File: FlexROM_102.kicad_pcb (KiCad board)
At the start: 2 copper layers, 16.4 x 34.2 mm, 5 parts, among them J1 27C256 DIP LEGS, U1 28C256

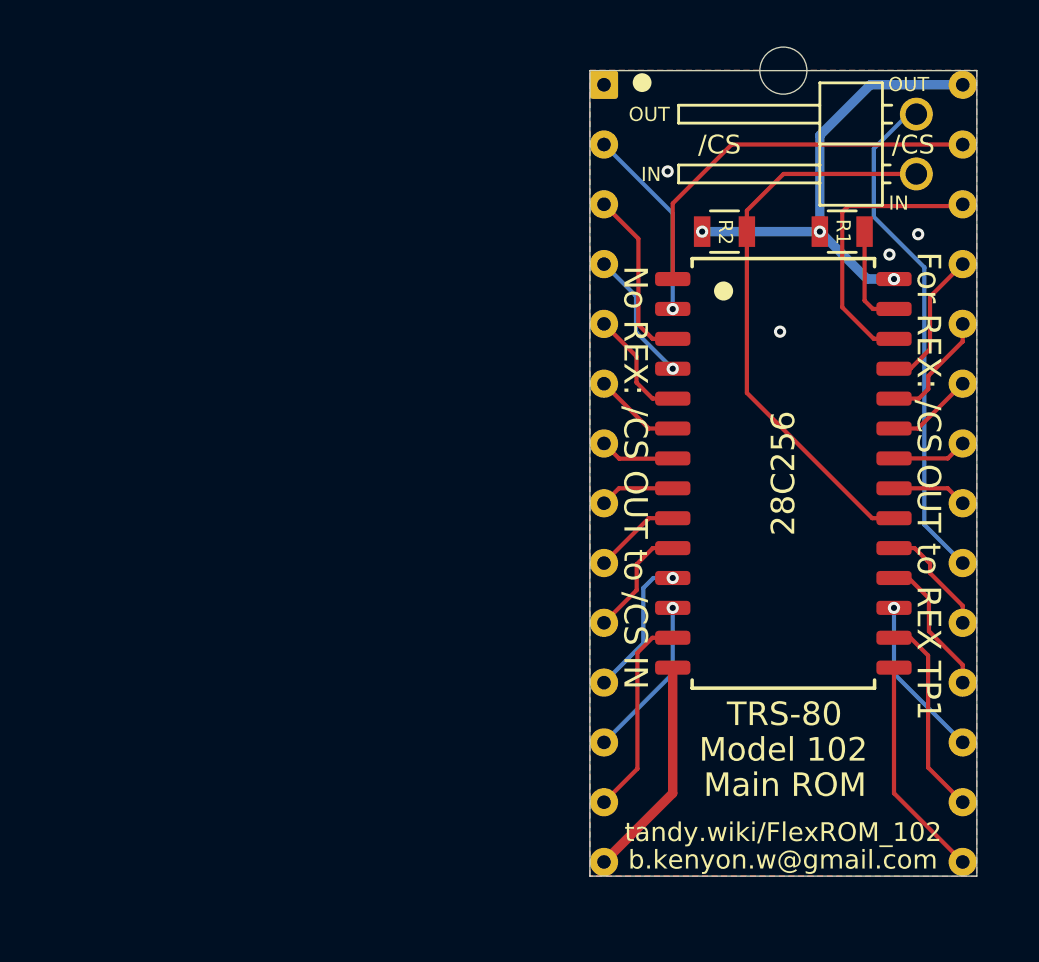
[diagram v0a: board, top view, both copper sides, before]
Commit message: FlexROM_100 programming adapter, FlexROM_102 programming jumpers
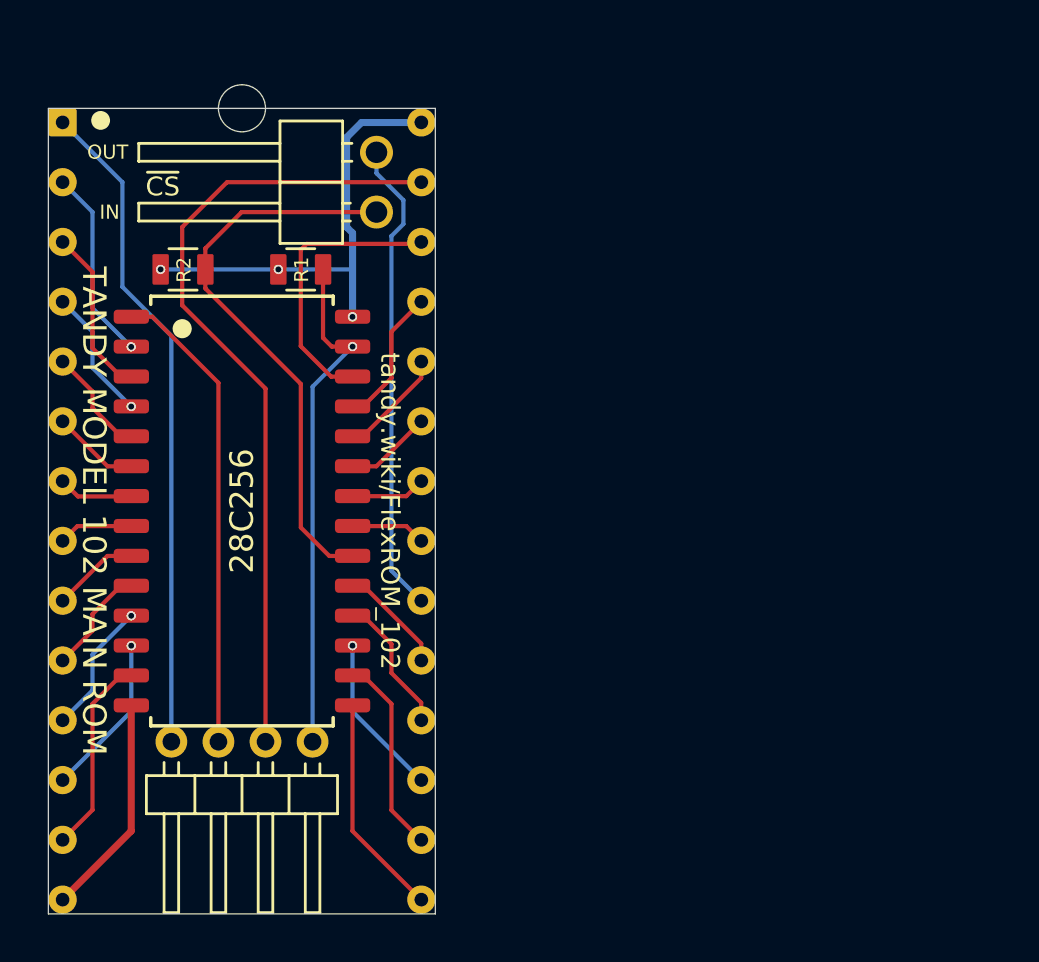
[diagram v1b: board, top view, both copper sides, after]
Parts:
- added JP2: Jumper_4_Bridged23, 000_LOCAL:PinHeader_1x04_P2.00mm_Horizontal, F.Cu at (130.0, 111.4)
- J1: footprint 000_LOCAL:DIP-28_W15.24mm_pcb_sil_pins -> 000_LOCAL:DIP28_0.6_pcb_sil_pins
- JP1: value /CS breakout (REX TP1) -> ~CS~ breakout (REX TP1)
- moved R1 23.1 mm to (129.5, 91.3)
- moved R2 23.1 mm to (124.5, 91.3)
- moved J1 23.1 mm to (127.0, 101.6)
- moved U1 23.1 mm to (127.0, 101.6)
- moved JP1 23.0 mm to (132.7, 88.9)
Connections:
- J1 pad 1: (no net) -> /NC_A14
- J1 pad 27: /A14 -> /A14_~WE
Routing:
- net /A14_~WE: track 0.00 -> 34.3 mm
- net /NC_A14: track 0.00 -> 28.2 mm
- net /~WE: track 4.33 -> 21.8 mm, vias 0 -> 1
- net /A14: track 16.6 -> 20.1 mm
- net /~CS_OUT: track 21.6 -> 20.3 mm
- net /VCC: track 20.0 -> 21.3 mm
- net /GND: vias 4 -> 0
- removed copper zone on B.Cu, net /GND
- removed copper zone on F.Cu, net /GND
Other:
- net class Default: clearance 0.2 -> 0.16; trace_width 0.25 -> 0.18; via_dia 0.8 -> 0.4; via_drill 0.4 -> 0.25
- rule trace_clearance: 0.2 -> 0.16
- rule via_min_drill: 0.26 -> 0.25
- rule via_min_size: 0.52 -> 0.4
- board text added: "PROGRAM"
- board text added: "RUN"
- board text added: "TANDY MODEL 102 MAIN ROM"
- board text added: "~CS"
- board text removed: "/CS"
- board text removed: "Connect /CS OUT to REX TP1. Leave /CS IN unconnected."
- board text removed: "For REX: /CS OUT to REX TP1"
- board text removed: "If REX is later removed, connect /CS OUT to /CS IN."
- board text removed: "Install a shunt on /CS, or, install wires as above,"
- board text removed: "Main ROM"
- board text removed: "Model 102"
- board text removed: "No REX: /CS OUT to /CS IN"
- board text removed: "REX can then be added later without disassembling."
- board text removed: "Run 2 wires from /CS IN & /CS OUT to Option ROM compartment."
- board text removed: "TRS-80"
- board text removed: "To use REX Main ROM feature:"
- board text removed: "To use without REX:"
- board text removed: "and connect them to each other in the Option ROM compartment."
- board text removed: "b.kenyon.w@gmail.com"

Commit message: silkscreen
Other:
- board text added: "REX main rom: ~CS~ OUT to REX TP1 No REX: ~CS~ OUT to ~CS~ IN"
- board text added: "To program: Set jumpers to PROGRAM. Put board in programmer. Set programmer for 28C256."
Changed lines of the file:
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@@
   (general
     (thickness 1.6)
-    (drawings 30)
+    (drawings 33)
     (tracks 132)
     (zones 0)
@@
     (35 F.Paste user hide)
     (36 B.SilkS user)
-    (37 F.SilkS user hide)
+    (37 F.SilkS user)
     (38 B.Mask user)
     (39 F.Mask user)
@@
       (rotate (xyz 0 0 0))
     )
+  )
+  (gr_text RUN (at 126.95 116.65 -90) (layer F.SilkS)
+    (effects (font (size 1 1) (thickness 0.15)))
+  )
+  (gr_text "To program:\n  Set jumpers to PROGRAM.\n  Put board in programmer.\n  Set programmer for 28C256." (at 127 84.6 90) (layer B.SilkS)
+    (effects (font (size 1 1) (thickness 0.15)) (justify left mirror))
+  )
+  (gr_text "REX main rom: ~CS~ OUT to REX TP1\nNo REX: ~CS~ OUT to ~CS~ IN" (at 121.7 84.5 -270) (layer B.SilkS)
+    (effects (font (size 1 1) (thickness 0.15)) (justify left mirror))
   )
   (gr_poly (pts (xy 124.3 113.8) (xy 123.7 113.8) (xy 123.7 113.2) (xy 124.3 113.2)) (layer B.SilkS) (width 0.1))
@@
   (segment (start 125.445 90.4418) (end 125.445 91.335) (width 0.18) (layer F.Cu) (net 28))
   (segment (start 132.715 88.9) (end 126.9868 88.9) (width 0.18) (layer F.Cu) (net 28))
+  (segment (start 130.71 103.51) (end 131.695 103.51) (width 0.18) (layer F.Cu) (net 28))
+  (segment (start 129.5 96.3) (end 129.5 102.3) (width 0.18) (layer F.Cu) (net 28))
   (segment (start 129.5 102.3) (end 130.71 103.51) (width 0.18) (layer F.Cu) (net 28))
-  (segment (start 129.5 96.2) (end 129.5 102.3) (width 0.18) (layer F.Cu) (net 28))
-  (segment (start 130.71 103.51) (end 131.695 103.51) (width 0.18) (layer F.Cu) (net 28))
-  (segment (start 125.445 92.145) (end 129.5 96.2) (width 0.18) (layer F.Cu) (net 28))
-  (segment (start 125.445 91.335) (end 125.445 92.145) (width 0.18) (layer F.Cu) (net 28))
+  (segment (start 125.445 92.245) (end 129.5 96.3) (width 0.18) (layer F.Cu) (net 28))
+  (segment (start 125.445 91.335) (end 125.445 92.245) (width 0.18) (layer F.Cu) (net 28))
   (segment (start 130.445 91.335) (end 130.445 91.335) (width 0.18) (layer F.Cu) (net 29))
   (segment (start 131.7 94.615) (end 131.695 94.62) (width 0.18) (layer F.Cu) (net 29))

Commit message: minor tidying
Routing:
- net /D0: track 5.65 -> 5.92 mm, vias 1 -> 0
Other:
- board text added: "~CS~ (to REX)"
- board text removed: "~CS"

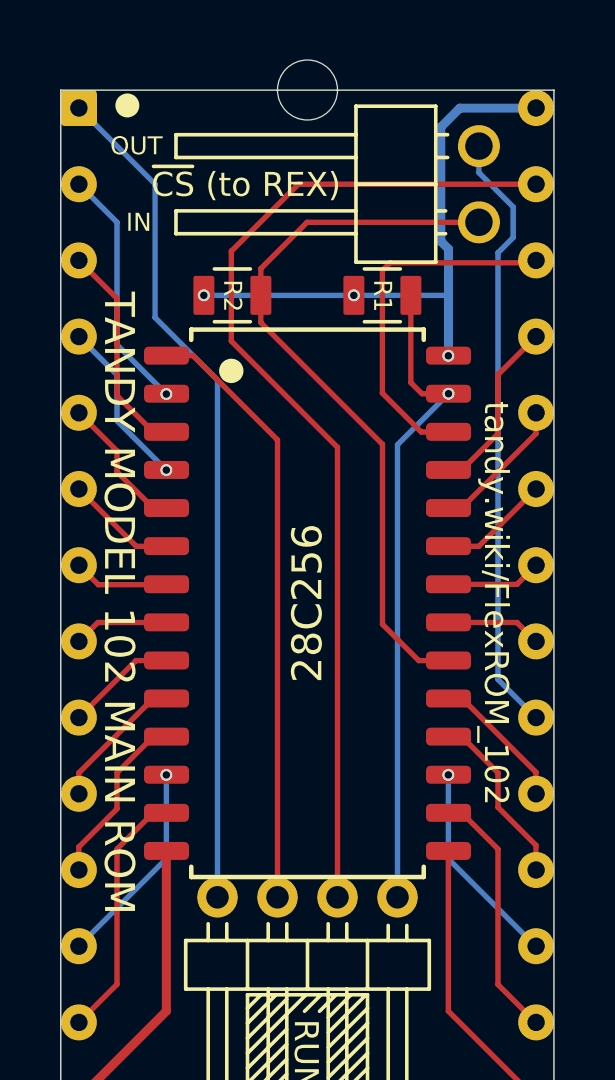
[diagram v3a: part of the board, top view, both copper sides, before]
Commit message: Add FlashROM_100. /WE pin on FlexROM_100
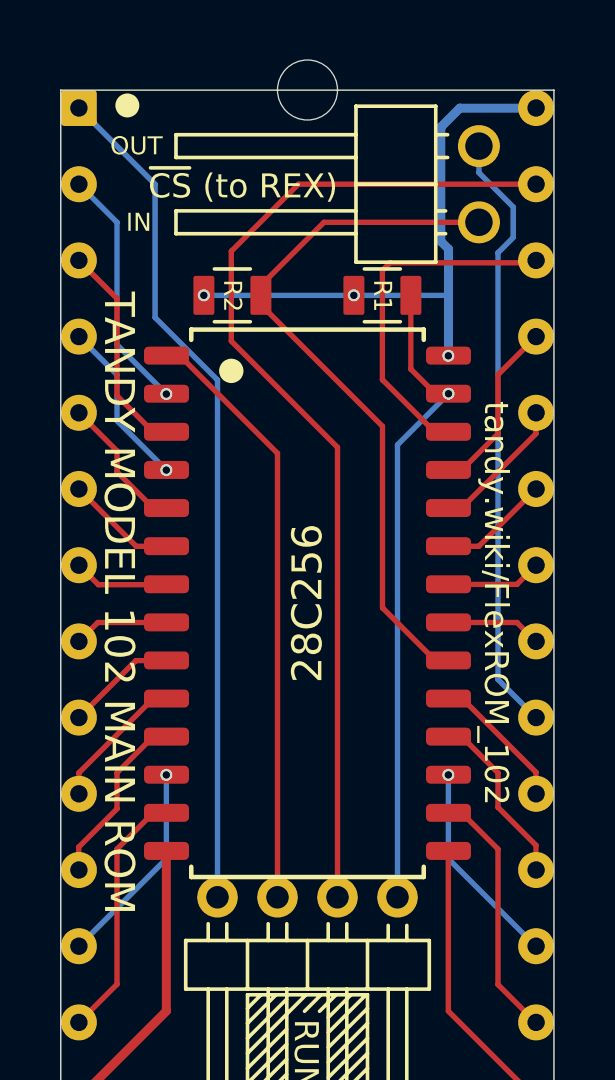
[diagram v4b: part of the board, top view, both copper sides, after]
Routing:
- net /~CS_IN: track 24.1 -> 23.5 mm

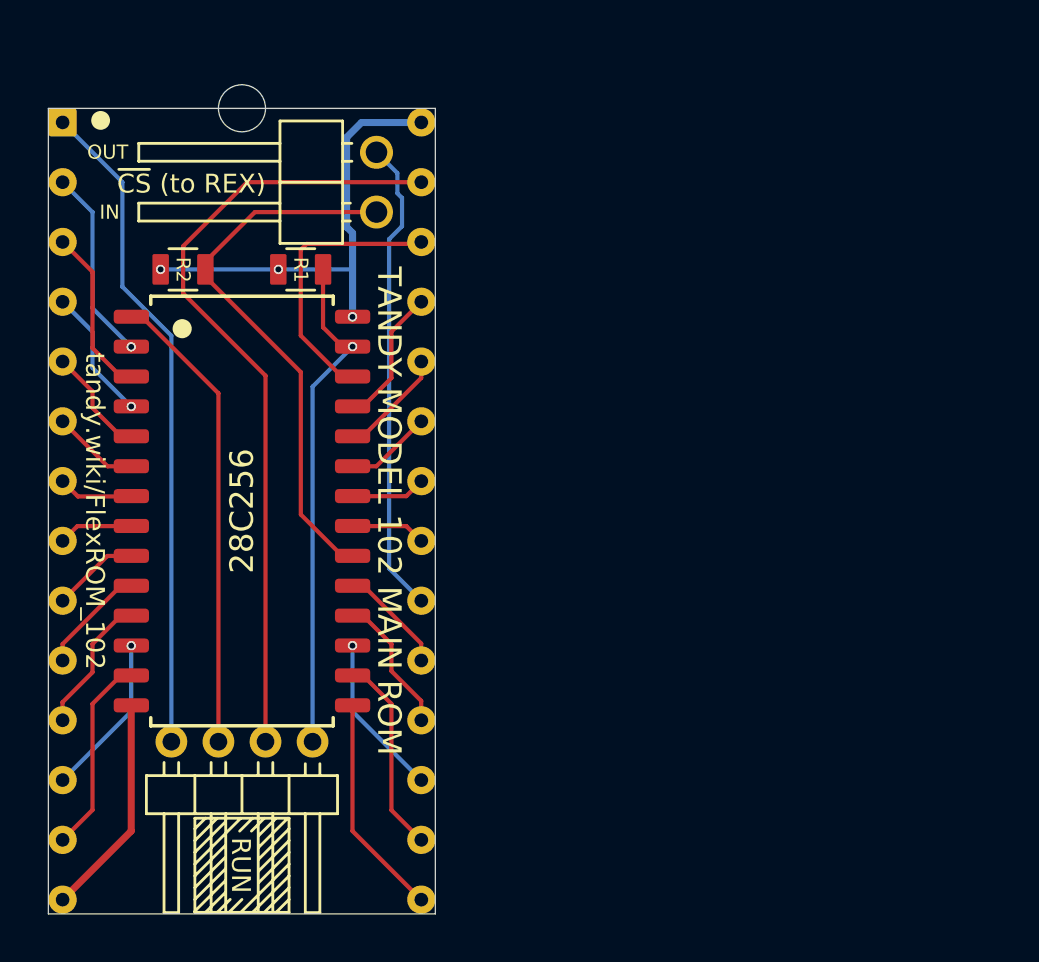
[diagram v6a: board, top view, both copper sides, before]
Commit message: simpler programming adapters, update pics and BOMs
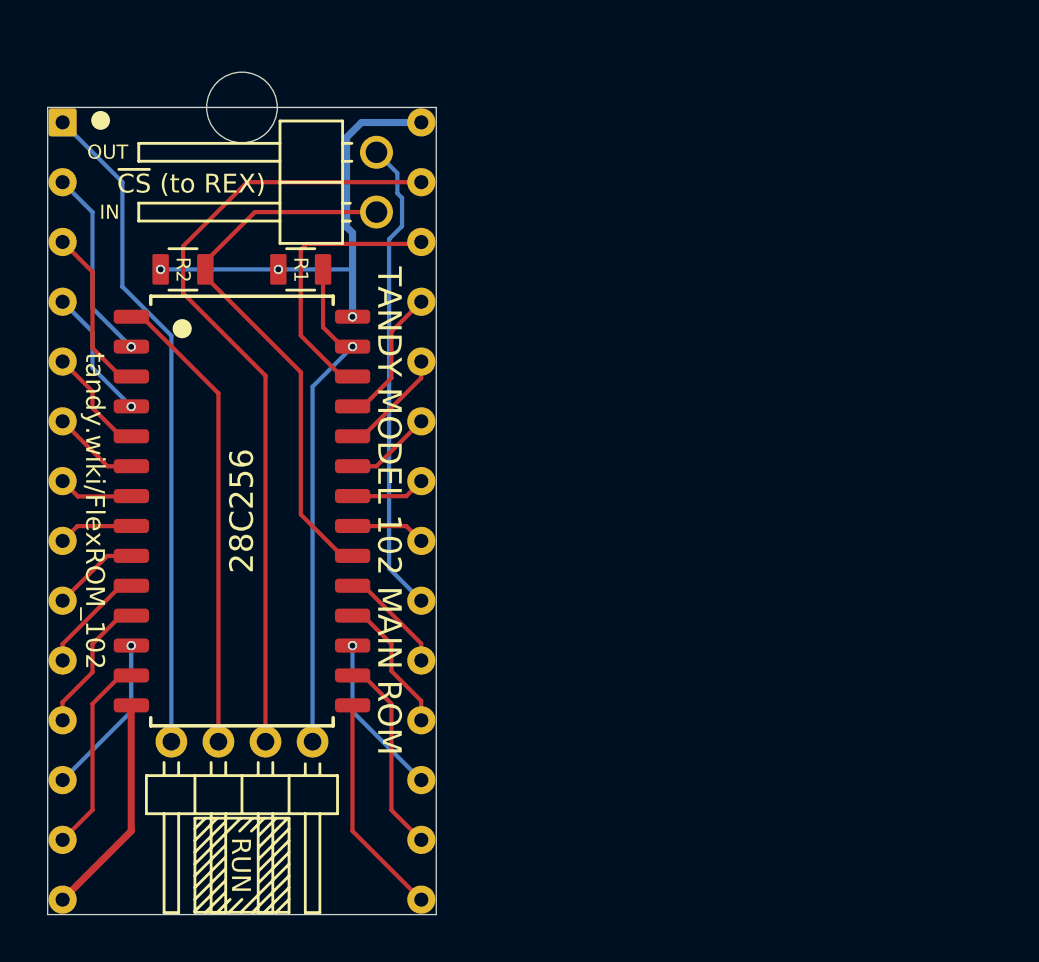
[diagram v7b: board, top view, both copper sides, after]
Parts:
- added REF**: NPTH_3mm, 000_LOCAL:NPTH_3mm, F.Cu at (127.0, 84.5)
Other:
- board size 16.4 x 34.2 mm -> 16.5 x 34.3 mm
